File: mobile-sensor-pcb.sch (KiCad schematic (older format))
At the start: 93 parts, among them J1 SMA, J2 USB_OTG, J3 JST PH, Q1 PNP-BJT-BIASED_SOT, SW1 RESET, SW2 ON/OFF, U1 3M_2908-05WB-MG, U10 LP2980AIM5-3.3/NOPB, U11 LP2980AIM5-3.3/NOPB, U12 LP2980AIM5-3.3/NOPB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

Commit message: More routing
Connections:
- net BATT-5V: now also C1.1
- net XBEE-3V3: now also C2.1
- net at C11.1, C13.1, J3.1 (P1)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: now also R24.1
- net at C20.1, C21.1, F1.2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: now also R23.1
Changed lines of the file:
@@
-$EndComp
-$Comp
-L C_Small C2
-U 1 1 55FAE430
-P 11900 7750
-F 0 "C2" H 11910 7820 50  0000 L CNN
-F 1 "10uF" H 11910 7670 50  0000 L CNN
-F 2 "Capacitors_SMD:C_1206_HandSoldering" H 11900 7750 60  0001 C CNN
-F 3 "" H 11900 7750 60  0000 C CNN
-	1    11900 7750
-	1    0    0    -1
 $EndComp
 $Comp
@@
 F 3 "" H 8600 1700 60  0000 C CNN
 	1    8600 1700
-	1    0    0    -1
-$EndComp
-$Comp
-L R_Small R24
-U 1 1 56035D61
-P 5775 2000
-F 0 "R24" H 5805 2020 50  0000 L CNN
-F 1 "1.80M" H 5805 1960 50  0000 L CNN
-F 2 "Resistors_SMD:R_0805_HandSoldering" H 5775 2000 60  0001 C CNN
-F 3 "" H 5775 2000 60  0000 C CNN
-	1    5775 2000
 	1    0    0    -1
 $EndComp
@@
 	13800 5950 13900 5950
 Wire Wire Line
-	13900 5950 13900 4950
+	13900 4950 13900 5950
 Wire Wire Line
 	12550 4950 14925 4950
@@
 	13900 4500 13600 4500
 Wire Wire Line
-	15550 3700 15400 3700
+	15400 3700 15550 3700
 Wire Wire Line
 	15950 3125 15950 3700
@@
 	5450 1900 5450 1950
 Connection ~ 5450 1900
-Wire Wire Line
-	5775 2100 5775 2300
 Wire Wire Line
 	5075 2150 5075 2350
@@
 Wire Wire Line
 	7575 2100 7626 2100
-Connection ~ 5774 1898
 Connection ~ 3600 3795
 Connection ~ 3600 5997
 Connection ~ 3750 8274
-Connection ~ 10296 7647
-Connection ~ 11901 7650
 Connection ~ 12250 7650
 Connection ~ 14120 4950
@@
 NoConn ~ 14550 3850
 $Comp
-L GND #PWR?
+L GND #PWR051
 U 1 1 560788C4
 P 850 2175
-F 0 "#PWR?" H 850 1925 50  0001 C CNN
+F 0 "#PWR051" H 850 1925 50  0001 C CNN
 F 1 "GND" H 850 2025 50  0000 C CNN
 F 2 "" H 850 2175 60  0000 C CNN
@@
 	1    0    0    -1
 $EndComp
+Wire Wire Line
+	5775 1925 5775 1900
+Connection ~ 5775 1900
+Wire Wire Line
+	5775 2125 5775 2300
+$Comp
+L R_Small R24
+U 1 1 560F98AA
+P 5775 2025
+F 0 "R24" H 5805 2045 50  0000 L CNN
+F 1 "1.80M" H 5805 1985 50  0000 L CNN
+F 2 "Resistors_SMD:R_0805_HandSoldering" H 5775 2025 60  0001 C CNN
+F 3 "" H 5775 2025 60  0000 C CNN
+	1    5775 2025
+	1    0    0    -1
+$EndComp
+Connection ~ 8600 1600
+$Comp
+L C_Small C2
+U 1 1 560FD67E
+P 11900 7750
+F 0 "C2" H 11910 7820 50  0000 L CNN
+F 1 "10uF" H 11910 7670 50  0000 L CNN
+F 2 "Capacitors_SMD:C_1206_HandSoldering" H 11900 7750 60  0001 C CNN
+F 3 "" H 11900 7750 60  0000 C CNN
+	1    11900 7750
+	1    0    0    -1
+$EndComp
+Connection ~ 11900 7650
+Connection ~ 10300 7650
 $EndSCHEMATC

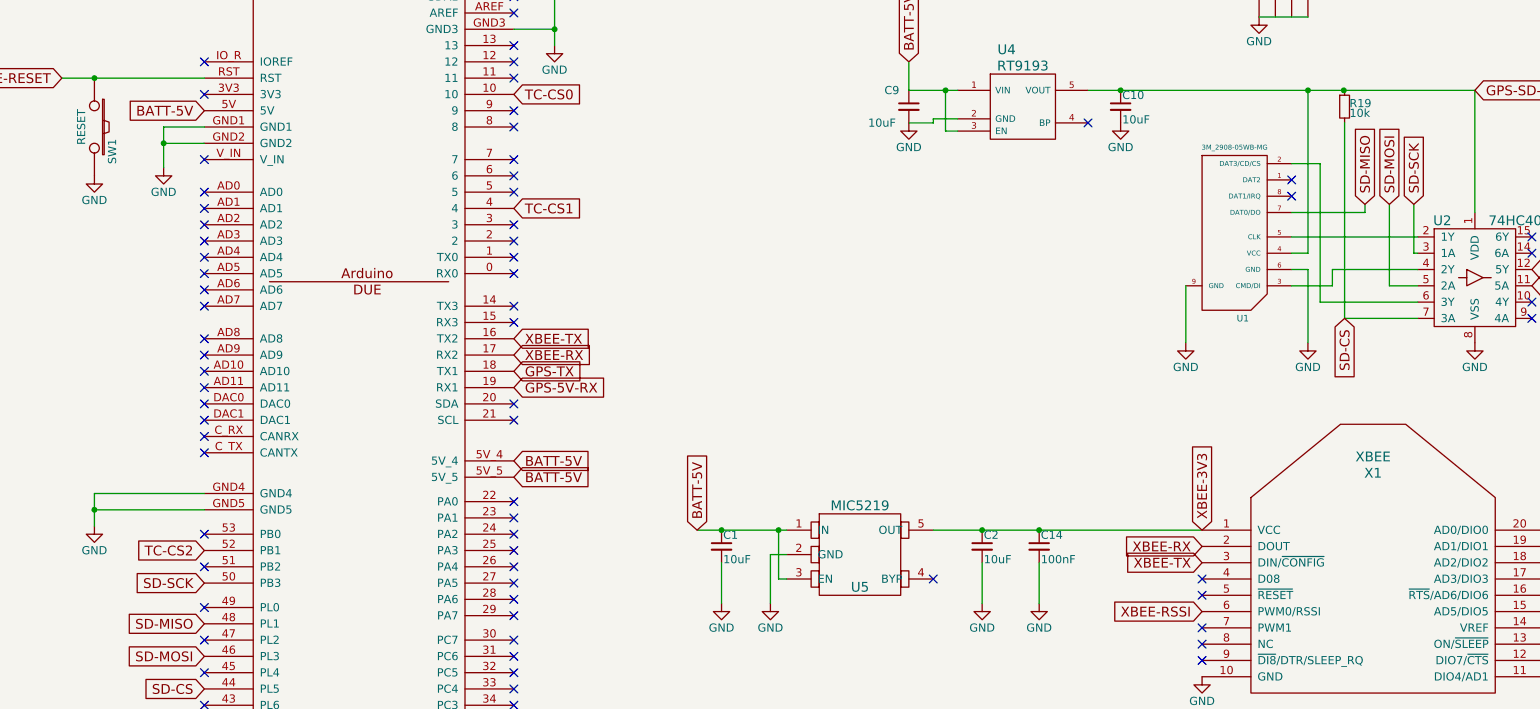
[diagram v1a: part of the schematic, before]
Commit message: Route all but thermocouples. Add LED arc screenshots.
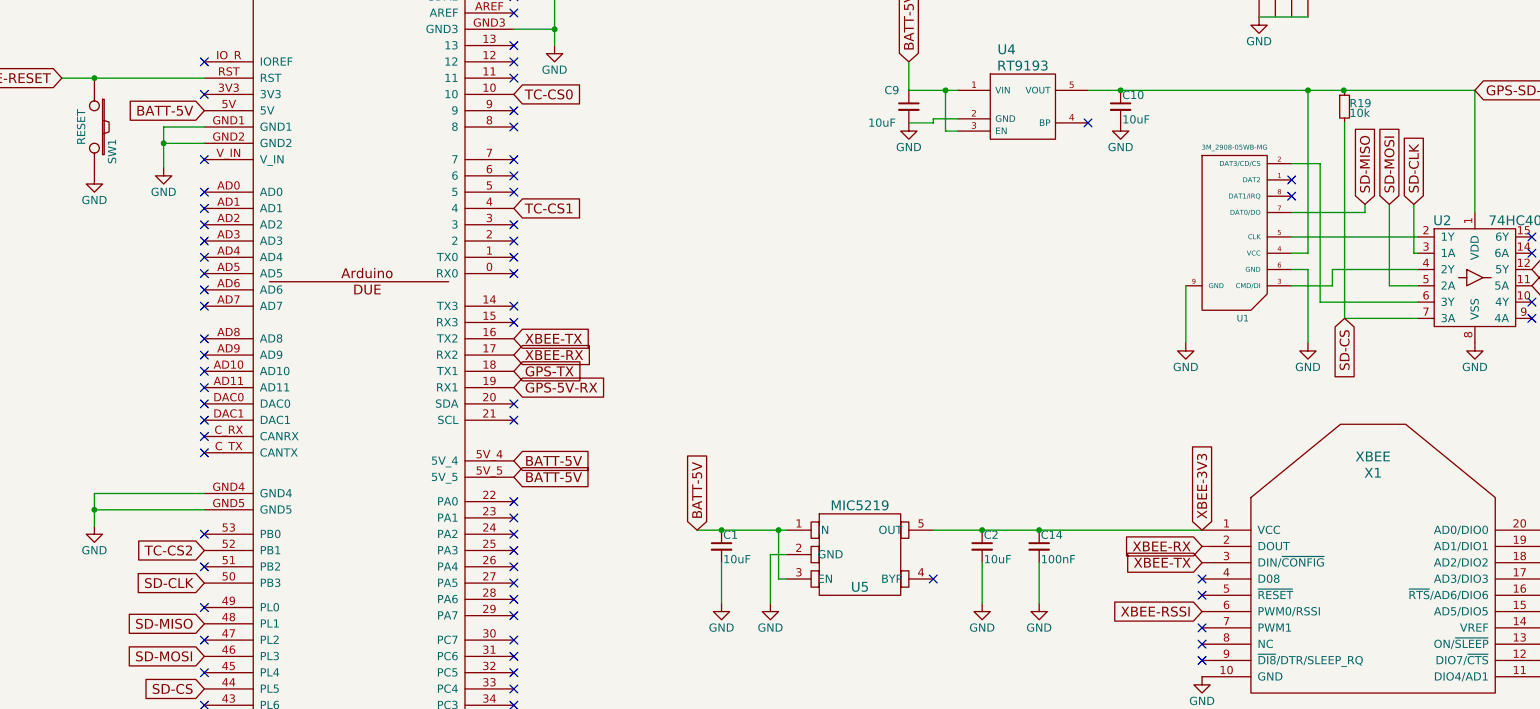
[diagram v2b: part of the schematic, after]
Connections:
- net SD-SCK is gone; now on net SD-CLK: SHIELD1.50 (PB3), U2.3 (1A)
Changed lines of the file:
@@
 BATT-5V
 Text GLabel 14550 5650 1    60   Input ~ 0
-SD-SCK
+SD-CLK
 Text GLabel 14400 5650 1    60   Input ~ 0
 SD-MOSI
@@
 SD-MOSI
 Text GLabel 7125 7975 0    60   Input ~ 0
-SD-SCK
+SD-CLK
 Text GLabel 7125 8625 0    60   Input ~ 0
 SD-CS

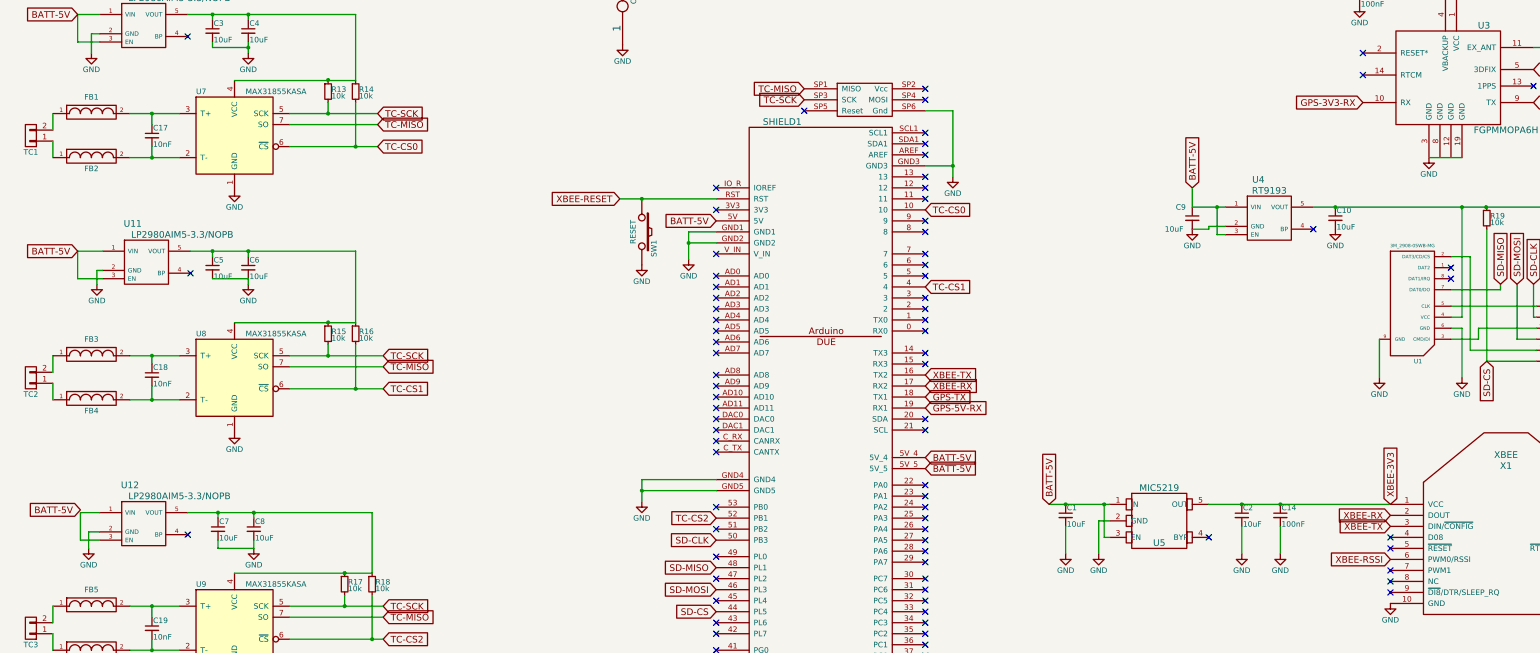
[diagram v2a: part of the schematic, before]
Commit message: Minor PCB fixes. Rework BOM to have fewer distributors. Change battery holder part.
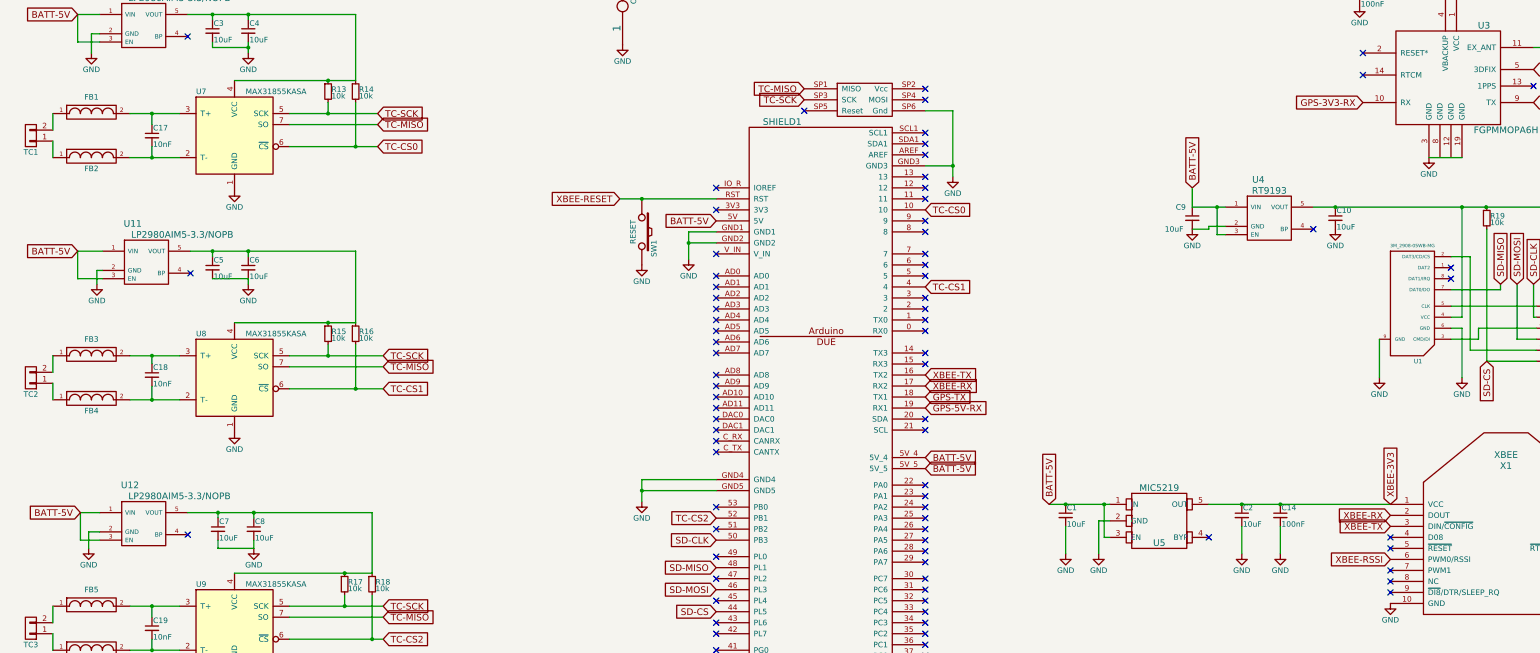
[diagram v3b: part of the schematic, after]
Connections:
- net BATT-5V: now also U12.1 (VIN), U12.3 (EN)
- net at C3.1, C4.1, R14.1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: now also R13.1
- net at C5.1, C6.1, R16.1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: now also R15.1
- net at C7.1, C8.1, R18.1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: now also R17.1
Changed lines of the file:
@@
-$EndComp
-$Comp
-L R_Small R15
-U 1 1 55FB3AEF
-P 3600 6100
-F 0 "R15" H 3630 6120 50  0000 L CNN
-F 1 "10k" H 3630 6060 50  0000 L CNN
-F 2 "Resistors_SMD:R_0805_HandSoldering" H 3600 6100 60  0001 C CNN
-F 3 "" H 3600 6100 60  0000 C CNN
-	1    3600 6100
-	1    0    0    -1
 $EndComp
 $Comp
@@
 	1    0    0    -1
 $EndComp
-Text GLabel 1350 7700 0    60   Input ~ 0
+Text GLabel 1350 7725 0    60   Input ~ 0
 BATT-5V
 Text GLabel 4100 8575 2    60   Input ~ 0
@@
 	13800 5950 13900 5950
 Wire Wire Line
-	13900 4950 13900 5950
+	13900 5950 13900 4950
 Wire Wire Line
 	12550 4950 14925 4950
@@
 Wire Wire Line
 	7575 2100 7626 2100
-Connection ~ 3600 3795
-Connection ~ 3600 5997
-Connection ~ 3750 8274
 Connection ~ 12250 7650
 Connection ~ 14120 4950
@@
 Connection ~ 11900 7650
 Connection ~ 10300 7650
+Connection ~ 3750 8275
+$Comp
+L R_Small R15
+U 1 1 55FB3AEF
+P 3600 6100
+F 0 "R15" H 3630 6120 50  0000 L CNN
+F 1 "10k" H 3630 6060 50  0000 L CNN
+F 2 "Resistors_SMD:R_0805_HandSoldering" H 3600 6100 60  0001 C CNN
+F 3 "" H 3600 6100 60  0000 C CNN
+	1    3600 6100
+	1    0    0    -1
+$EndComp
+Connection ~ 3600 6000
+Connection ~ 3600 3800
 $EndSCHEMATC

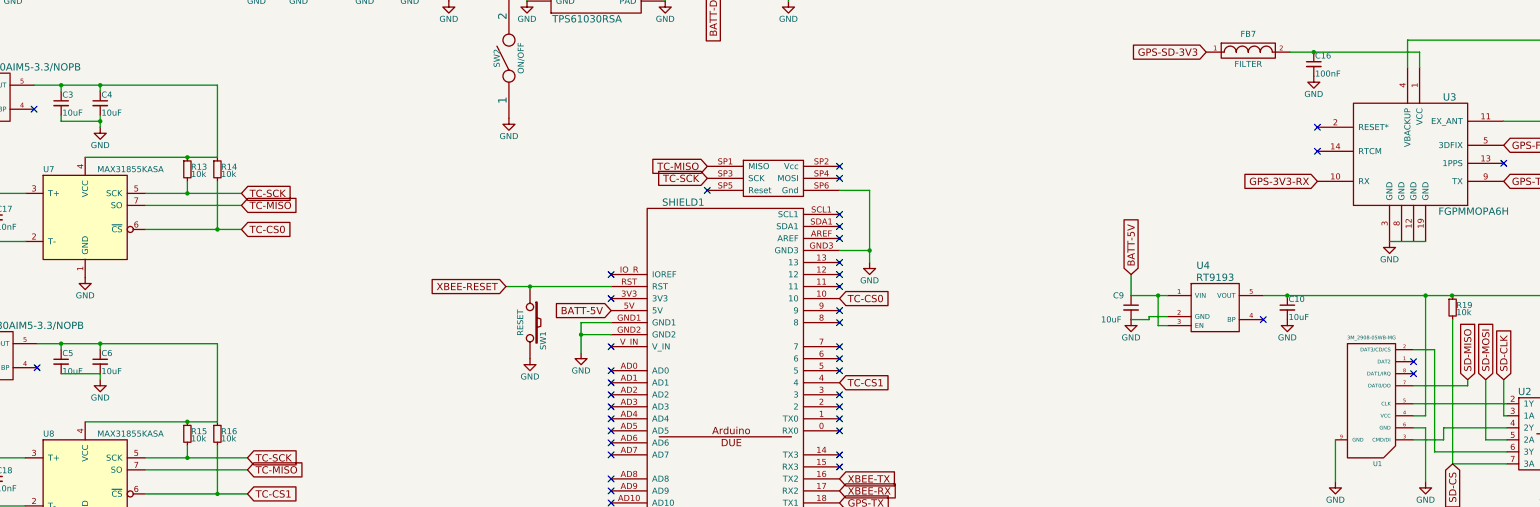
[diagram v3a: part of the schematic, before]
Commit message: Fix a R19 connection, spin SD card holder, fix SMA jack
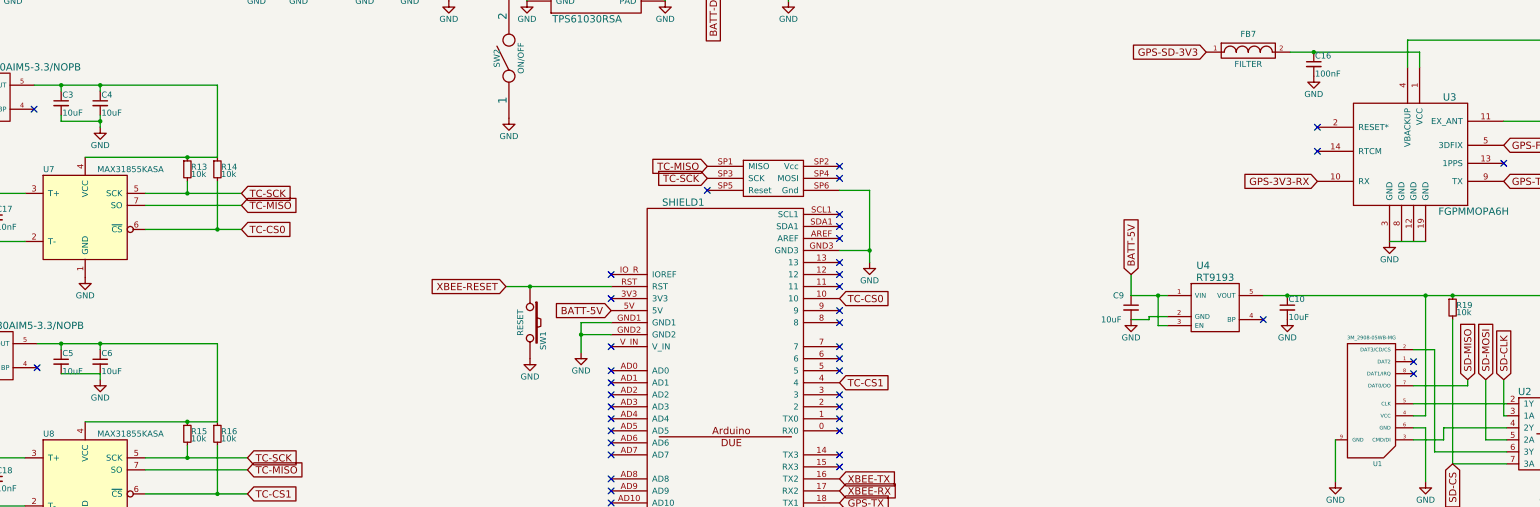
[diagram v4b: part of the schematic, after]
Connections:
- net GPS-SD-3V3: now also R19.1
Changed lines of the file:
@@
 EESchema Schematic File Version 2
-LIBS:mobile-sensor-pcb-rescue
 LIBS:rascalmicro-kicad-library
 LIBS:power
@@
 	13800 5950 13900 5950
 Wire Wire Line
-	13900 5950 13900 4950
+	13900 4950 13900 5950
 Wire Wire Line
 	12550 4950 14925 4950
@@
 Connection ~ 2875 3500
 Wire Wire Line
-	3850 3200 3850 3800
+	3850 3800 3850 3200
 Connection ~ 2875 3200
 Wire Wire Line
-	3850 3800 2750 3800
+	2750 3800 3850 3800
 Wire Wire Line
 	1100 6550 1100 6700
@@
 	2875 5600 2875 5650
 Wire Wire Line
-	3850 5350 3850 6000
+	3850 6000 3850 5350
 Connection ~ 2875 5350
 Wire Wire Line
-	3850 6000 2750 6000
+	2750 6000 3850 6000
 Wire Wire Line
 	3250 6300 4100 6300
@@
 	7575 2100 7626 2100
 Connection ~ 12250 7650
-Connection ~ 14120 4950
 Connection ~ 12970 2925
 Connection ~ 15450 3700
@@
 Connection ~ 3600 6000
 Connection ~ 3600 3800
+Connection ~ 14125 4950
 $EndSCHEMATC

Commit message: Add BOMs and what appear to be some final PCB changes
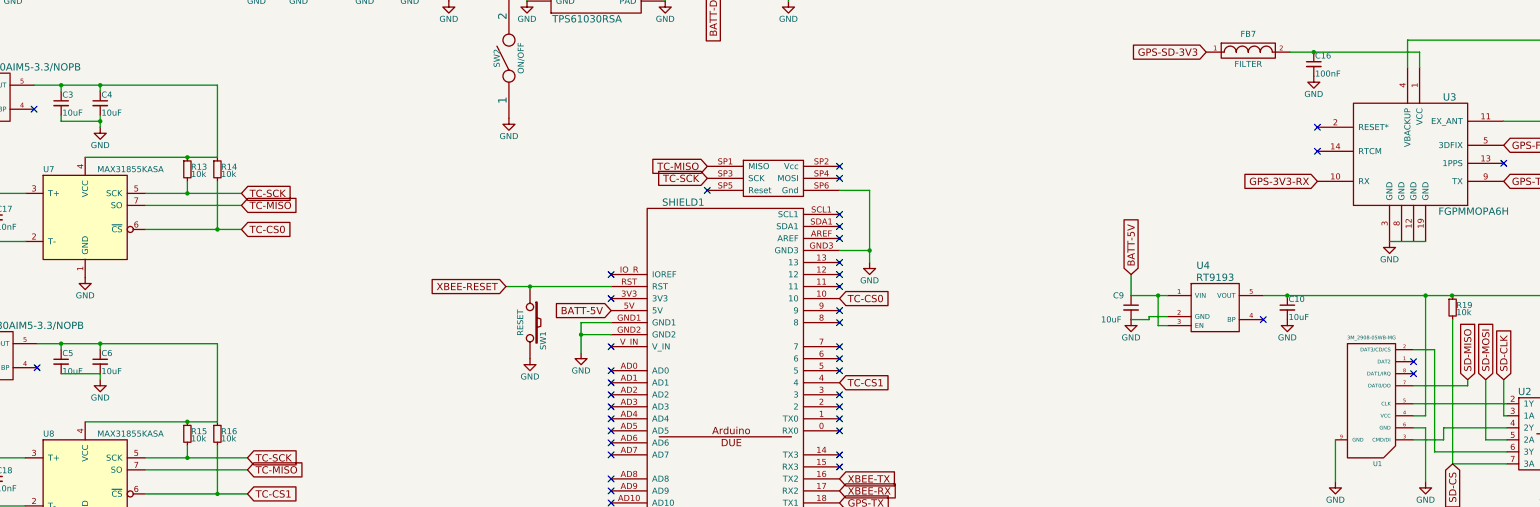
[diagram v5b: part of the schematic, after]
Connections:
- net GPS-SD-3V3: no longer R19.1
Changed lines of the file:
@@
 EESchema Schematic File Version 2
+LIBS:mobile-sensor-pcb-rescue
 LIBS:rascalmicro-kicad-library
 LIBS:power
@@
 	13800 5950 13900 5950
 Wire Wire Line
-	13900 4950 13900 5950
+	13900 5950 13900 4950
 Wire Wire Line
 	12550 4950 14925 4950
@@
 Connection ~ 2875 3500
 Wire Wire Line
-	3850 3800 3850 3200
+	3850 3200 3850 3800
 Connection ~ 2875 3200
 Wire Wire Line
-	2750 3800 3850 3800
+	3850 3800 2750 3800
 Wire Wire Line
 	1100 6550 1100 6700
@@
 	2875 5600 2875 5650
 Wire Wire Line
-	3850 6000 3850 5350
+	3850 5350 3850 6000
 Connection ~ 2875 5350
 Wire Wire Line
-	2750 6000 3850 6000
+	3850 6000 2750 6000
 Wire Wire Line
 	3250 6300 4100 6300
@@
 	7575 2100 7626 2100
 Connection ~ 12250 7650
+Connection ~ 14120 4950
 Connection ~ 12970 2925
 Connection ~ 15450 3700
@@
 Connection ~ 3600 6000
 Connection ~ 3600 3800
-Connection ~ 14125 4950
 $EndSCHEMATC
